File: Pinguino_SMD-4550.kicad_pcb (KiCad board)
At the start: 2 copper layers, 25.4 x 25.4 mm, 54 parts, among them P1 uUSB, P10 CONN_01X01, P11 CONN_01X01, P12 CONN_01X01, P13 CONN_01X01, P14 CONN_01X01, P15 CONN_01X01, P16 CONN_01X01, P17 CONN_01X01, P18 CONN_01X01, P19 CONN_01X01, P2 CONN_01X01, P20 CONN_01X01, P21 CONN_01X01, P22 CONN_01X01, P23 CONN_01X01, P24 CONN_01X01, P25 CONN_01X01, P26 CONN_01X01, P27 CONN_01X01, P28 CONN_01X01, P29 CONN_01X01, P3 CONN_01X01, P30 CONN_01X01, P31 CONN_01X01, P32 CONN_01X01, P33 CONN_01X01, P34 CONN_01X01, P35 CONN_01X01, P36 CONN_01X01, P37 CONN_01X01, P38 CONN_01X01, P39 CONN_01X01, P4 CONN_01X01, P40 CONN_01X01, P41 CONN_01X01, P5 CONN_01X01, P6 CONN_01X01, P7 CONN_01X01, P8 CONN_01X01, P9 CONN_01X01, SW1 Reset, U1 PIC18(L)F4550-I/PT, Y1 Crystal

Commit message: Tracks and Vias improvement
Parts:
- moved C5 0.18 mm to (78.1, 63.5)
- turned R2 to 180 degrees
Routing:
- net VCC: track 79.8 -> 71.9 mm, vias 0 -> 1
- net GND: track 95.2 -> 101.4 mm
- net /PIN27: track 16.7 -> 12.8 mm
- net /MCLR: track 15.6 -> 18.1 mm
- net /PIN18/A5: track 10.5 -> 12.7 mm, vias 0 -> 1
- net /PIN26: track 11.7 -> 13.6 mm
- net /PIN0/SDA: track 13.8 -> 14.9 mm
- net /ICSP-VPP: track 8.98 -> 8.21 mm
- net /PIN20/A7: track 14.4 -> 15.0 mm
- net /PIN1/SCL: track 13.7 -> 14.4 mm
- net /PIN8/TX: track 6.70 -> 6.71 mm, vias 0 -> 1

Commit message: Added zones (F.cu, B.cu -> GND)
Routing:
- added copper zone on B.Cu, net GND
- added copper zone on F.Cu, net GND
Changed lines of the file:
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@@
   (segment (start 92.9 54.8) (end 92.71 54.61) (width 0.254) (layer F.Cu) (net 44))
   (segment (start 92.9 57.8) (end 92.9 54.8) (width 0.254) (layer F.Cu) (net 44))
+  (zone (net 1) (net_name GND) (layer B.Cu) (hatch edge 0.508)
+    (connect_pads (clearance 0.3302))
+    (min_thickness 0.254)
+    (fill yes (arc_segments 16) (thermal_gap 0.508) (thermal_bridge_width 0.508))
+    (polygon
+      (pts
+        (xy 76.2 50.8) (xy 101.6 50.8) (xy 101.6 76.2) (xy 76.2 76.2)
+      )
+    )
+  )
+  (zone (net 1) (net_name GND) (layer F.Cu) (hatch edge 0.508)
+    (connect_pads (clearance 0.3302))
+    (min_thickness 0.254)
+    (fill yes (arc_segments 16) (thermal_gap 0.508) (thermal_bridge_width 0.508))
+    (polygon
+      (pts
+        (xy 76.2 50.8) (xy 101.6 50.8) (xy 101.6 76.2) (xy 76.2 76.2)
+      )
+    )
+  )
 )

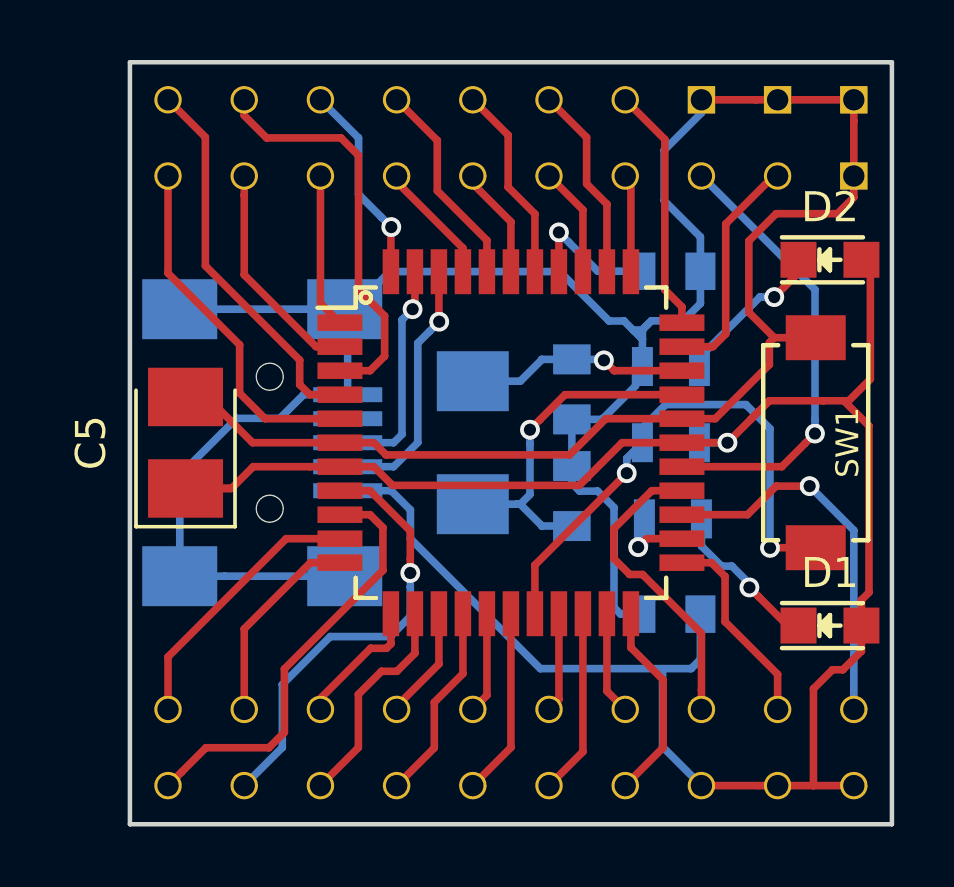
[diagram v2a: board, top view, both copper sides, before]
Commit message: Silkscreen layers
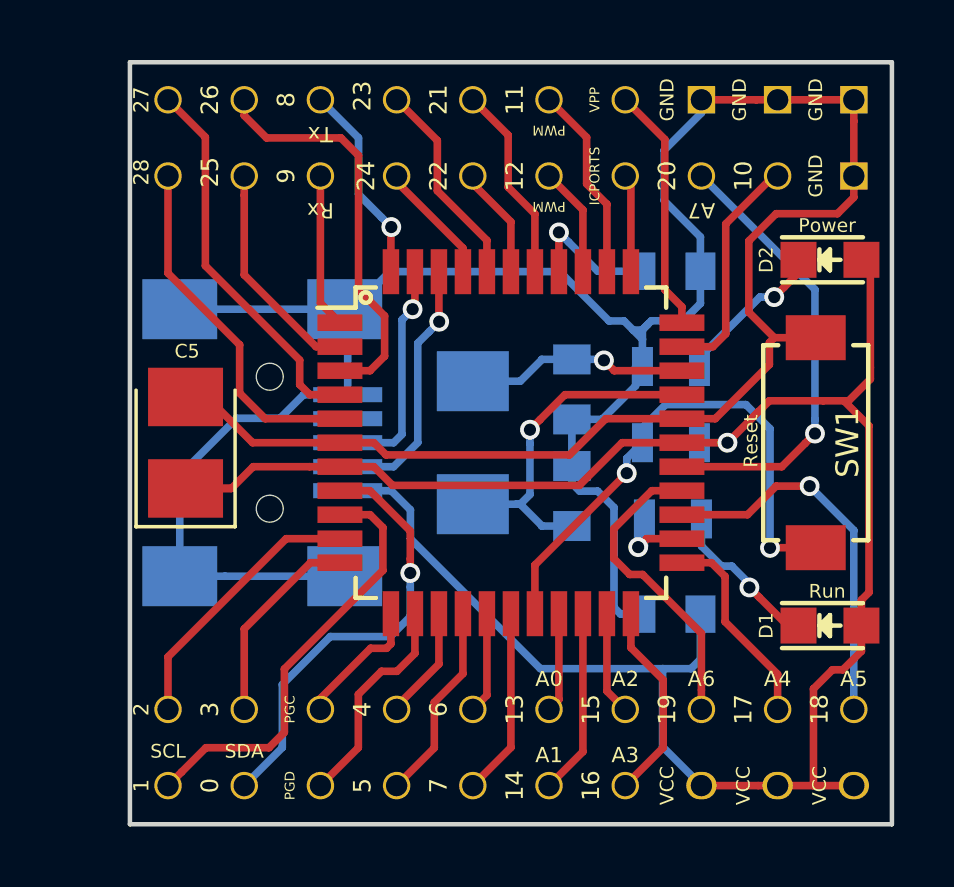
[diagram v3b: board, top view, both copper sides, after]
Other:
- rule pad_to_mask_clearance: 0.2 -> 0.1524
- board text added: "0"
- board text added: "1"
- board text added: "10"
- board text added: "11"
- board text added: "11 12"
- board text added: "12"
- board text added: "13"
- board text added: "13 14"
- board text added: "14"
- board text added: "15"
- board text added: "15 16"
- board text added: "16"
- board text added: "17"
- board text added: "17 VCC"
- board text added: "18"
- board text added: "18 VCC"
- board text added: "19"
- board text added: "19 VCC"
- board text added: "2"
- board text added: "2 1"
- board text added: "20"
- board text added: "21"
- board text added: "21 22"
- board text added: "22"
- board text added: "23"
- board text added: "23 24"
- board text added: "24"
- board text added: "25"
- board text added: "26"
- board text added: "26 25"
- board text added: "27"
- board text added: "27 28"
- board text added: "28"
- board text added: "3"
- board text added: "3 0"
- board text added: "4"
- board text added: "4 5"
- board text added: "5"
- board text added: "6"
- board text added: "6 7"
- board text added: "7"
- board text added: "8"
- board text added: "8 9"
- board text added: "9"
- board text added: "A0"
- board text added: "A0 A1"
- board text added: "A1"
- board text added: "A2"
- board text added: "A3"
- board text added: "A4"
- board text added: "A5"
- board text added: "A6"
- board text added: "A7"
- board text added: "GND"
- board text added: "GND 10"
- board text added: "GND 20"
- board text added: "GND GND"
- board text added: "ICPORTS"
- board text added: "PGC"
- board text added: "PGD"
- board text added: "PGD PGC"
- board text added: "PWM"
- board text added: "Power"
- board text added: "Run"
- board text added: "Rx"
- board text added: "SCL"
- board text added: "SDA"
- board text added: "Tx"
- board text added: "VCC"
- board text added: "VPP"
- board text added: "VPP Debug"

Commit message: Silkscreen layes: Logos
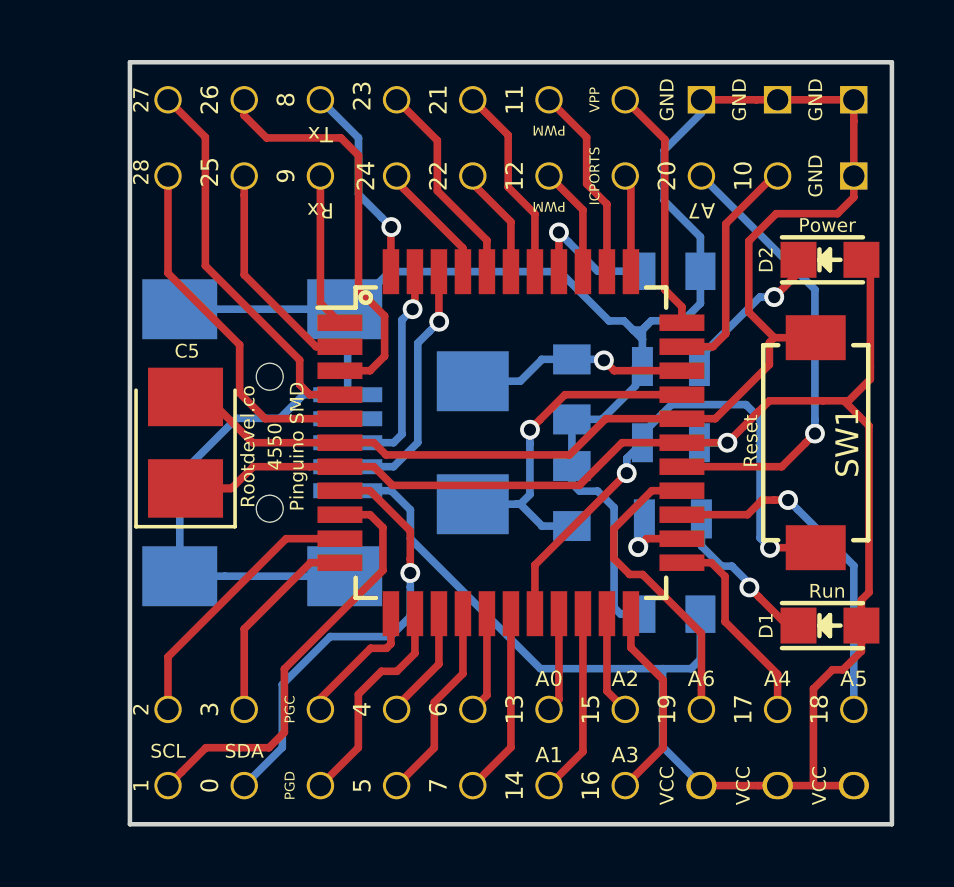
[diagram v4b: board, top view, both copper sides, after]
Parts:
- added G***: LOGO, LOGO, B.Cu at (98.8, 63.2)
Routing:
- net /PIN18/A5: track 12.7 -> 11.6 mm
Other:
- board text added: "4550 Pinguino SMD"
- board text added: "Rootdevel.co"
